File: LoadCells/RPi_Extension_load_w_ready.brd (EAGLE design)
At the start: 80 x 50 mm, 42 parts, among them U1 AD7730BRUZ, U2 AD7730BRUZ, U3 AD7730BRUZ, U4 AD7730BRUZ, U5 AD7730BRUZ, U6 AD7730BRUZ, U7 AD7730BRUZ, U8 AD7730BRUZ, U9 STM32F103RCT6, Y1 ABM3B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

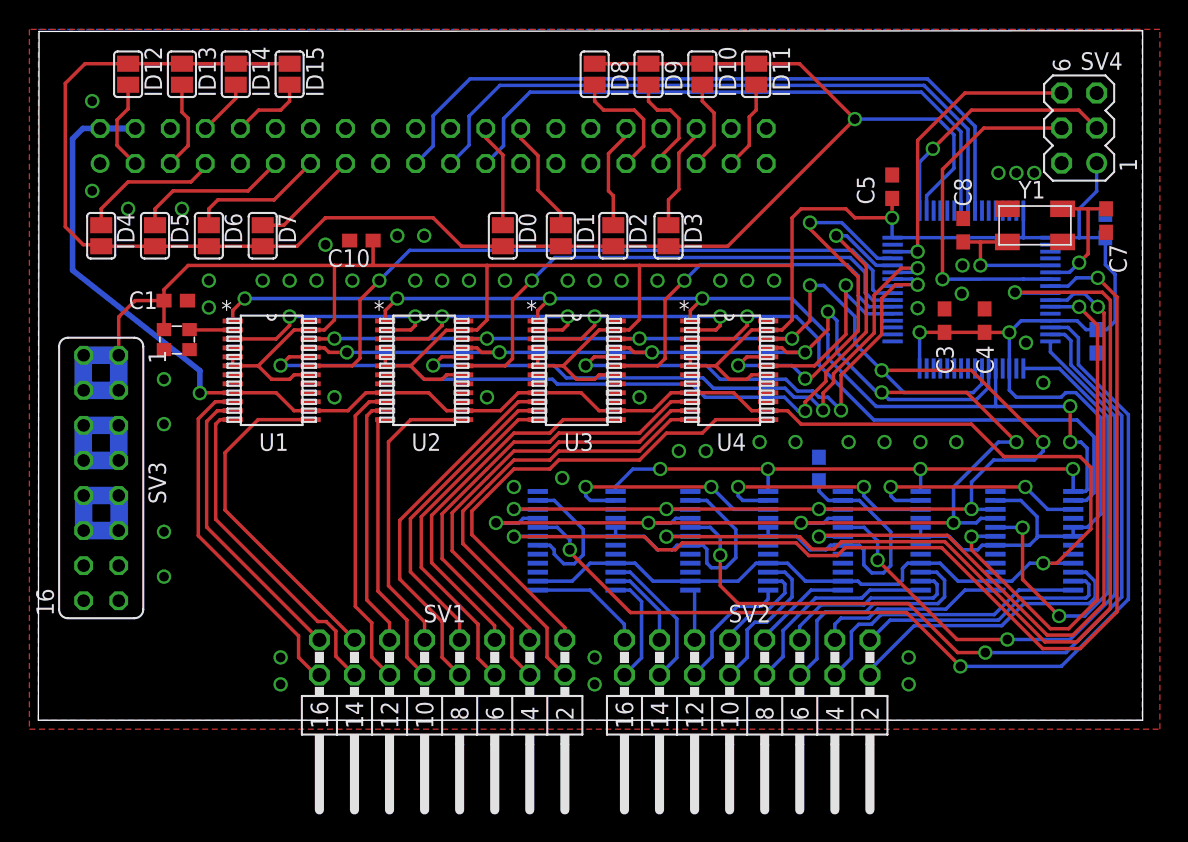
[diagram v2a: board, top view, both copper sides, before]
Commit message: added additional ground vias
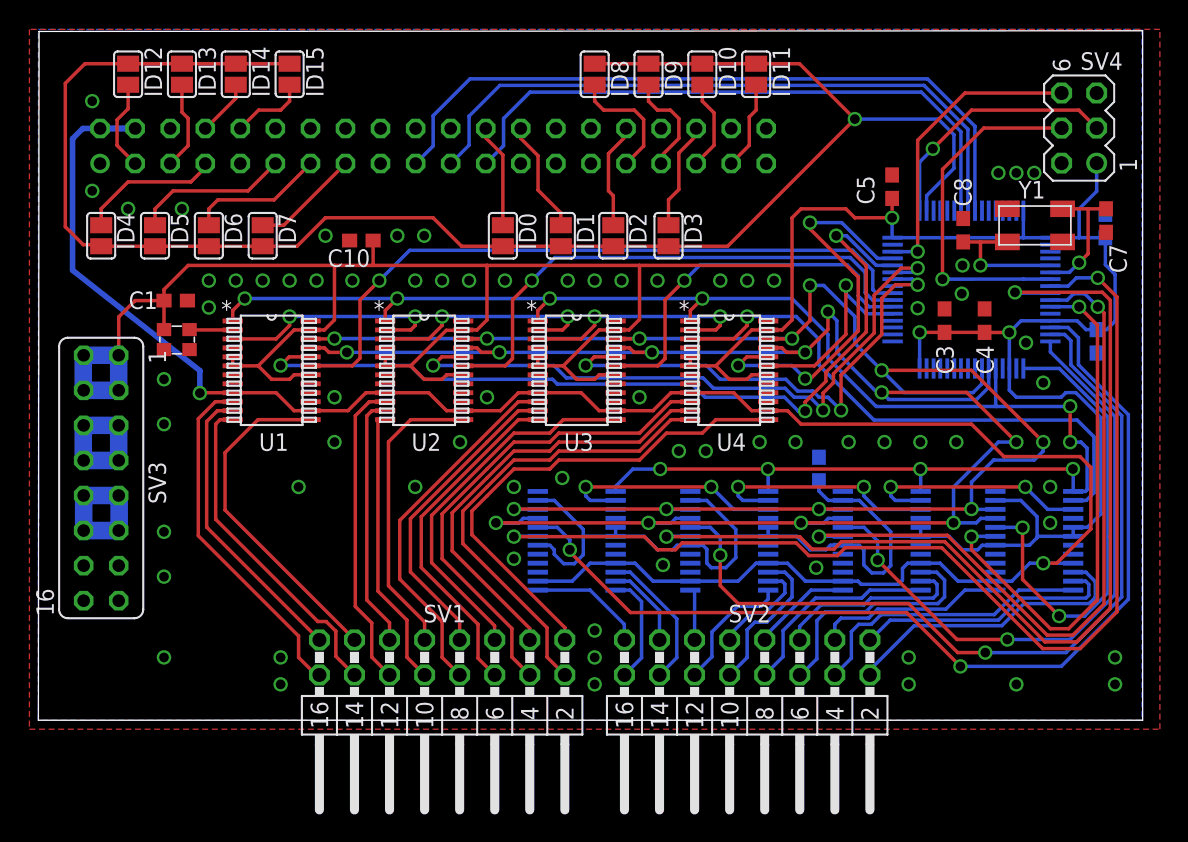
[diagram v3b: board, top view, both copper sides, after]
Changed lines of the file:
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@@
 </class>
 </classes>
-<designrules name="pban_4mil-l2">
-<description language="de">&lt;b&gt;EAGLE Design Rules&lt;/b&gt;
-&lt;p&gt;
-Die Standard-Design-Rules sind so gewählt, dass sie für
-die meisten Anwendungen passen. Sollte ihre Platine
-besondere Anforderungen haben, treffen Sie die erforderlichen
-Einstellungen hier und speichern die Design Rules unter
-einem neuen Namen ab.</description>
-<description language="en">&lt;b&gt;EAGLE Design Rules&lt;/b&gt;
-&lt;p&gt;
-The default Design Rules have been set to cover
-a wide range of applications. Your particular design
-may have different requirements, so please make the
-necessary adjustments and save your customized
-design rules under a new name.</description>
+<designrules name="dirt_cheap_dirty_boards.v1">
+<description language="en">&lt;b&gt;Dirty Cheap Dirty Board Design Rules&lt;/b&gt;
+&lt;br&gt;
+&lt;br&gt;Min width/Spacing: 5/5mil
+&lt;br&gt;Min diameter of finished hole 12mil</description>
 <param name="layerSetup" value="(1*16)"/>
-<param name="mtCopper" value="0.035mm 0.035mm 0.035mm 0.035mm 0.035mm 0.035mm 0.035mm 0.035mm 0.035mm 0.035mm 0.035mm 0.035mm 0.035mm 0.035mm 0.035mm 0.035mm"/>
-<param name="mtIsolate" value="1.53mm 1.5mm 0.2mm 0.15mm 0.2mm 0.15mm 0.2mm 0.15mm 0.2mm 0.15mm 0.2mm 0.15mm 0.2mm 0.15mm 0.2mm"/>
-<param name="mdWireWire" value="0.1mm"/>
-<param name="mdWirePad" value="0.229mm"/>
-<param name="mdWireVia" value="0.229mm"/>
-<param name="mdPadPad" value="0.1mm"/>
-<param name="mdPadVia" value="0.229mm"/>
-<param name="mdViaVia" value="0.1mm"/>
-<param name="mdSmdPad" value="0.1mm"/>
-<param name="mdSmdVia" value="0.1mm"/>
-<param name="mdSmdSmd" value="0.1mm"/>
-<param name="mdViaViaSameLayer" value="5mil"/>
+<param name="mtCopper" value="0.035mm 0.0175mm 0.035mm 0.035mm 0.035mm 0.035mm 0.035mm 0.035mm 0.035mm 0.035mm 0.035mm 0.035mm 0.035mm 0.035mm 0.0175mm 0.035mm"/>
+<param name="mtIsolate" value="1.5mm 1.1mm 0.2mm 0.15mm 0.2mm 0.15mm 0.2mm 0.15mm 0.2mm 0.15mm 0.2mm 0.15mm 0.2mm 0.15mm 0.2mm"/>
+<param name="mdWireWire" value="5mil"/>
+<param name="mdWirePad" value="5mil"/>
+<param name="mdWireVia" value="5mil"/>
+<param name="mdPadPad" value="5mil"/>
+<param name="mdPadVia" value="5mil"/>
+<param name="mdViaVia" value="5mil"/>
+<param name="mdSmdPad" value="0mil"/>
+<param name="mdSmdVia" value="0mil"/>
+<param name="mdSmdSmd" value="0mil"/>
+<param name="mdViaViaSameLayer" value="8mil"/>
 <param name="mnLayersViaInSmd" value="2"/>
-<param name="mdCopperDimension" value="0.5mm"/>
-<param name="mdDrill" value="0.5mm"/>
+<param name="mdCopperDimension" value="10mil"/>
+<param name="mdDrill" value="10mil"/>
 <param name="mdSmdStop" value="0mil"/>
-<param name="msWidth" value="0.1mm"/>
-<param name="msDrill" value="0.3mm"/>
-<param name="msMicroVia" value="0.1mm"/>
-<param name="msBlindViaRatio" value="0.76"/>
+<param name="msWidth" value="5mil"/>
+<param name="msDrill" value="12mil"/>
+<param name="msMicroVia" value="12mil"/>
+<param name="msBlindViaRatio" value="0.5"/>
 <param name="rvPadTop" value="0.25"/>
 <param name="rvPadInner" value="0.25"/>
@@
 <param name="rvMicroViaOuter" value="0.25"/>
 <param name="rvMicroViaInner" value="0.25"/>
-<param name="rlMinPadTop" value="0.15mm"/>
-<param name="rlMaxPadTop" value="0.5mm"/>
-<param name="rlMinPadInner" value="0.2mm"/>
-<param name="rlMaxPadInner" value="0.5mm"/>
-<param name="rlMinPadBottom" value="0.15mm"/>
-<param name="rlMaxPadBottom" value="0.5mm"/>
-<param name="rlMinViaOuter" value="0.15mm"/>
-<param name="rlMaxViaOuter" value="0.5mm"/>
-<param name="rlMinViaInner" value="0.2mm"/>
-<param name="rlMaxViaInner" value="0.5mm"/>
-<param name="rlMinMicroViaOuter" value="0.1mm"/>
-<param name="rlMaxMicroViaOuter" value="0.5mm"/>
-<param name="rlMinMicroViaInner" value="0.1mm"/>
-<param name="rlMaxMicroViaInner" value="0.5mm"/>
+<param name="rlMinPadTop" value="10mil"/>
+<param name="rlMaxPadTop" value="20mil"/>
+<param name="rlMinPadInner" value="10mil"/>
+<param name="rlMaxPadInner" value="20mil"/>
+<param name="rlMinPadBottom" value="10mil"/>
+<param name="rlMaxPadBottom" value="20mil"/>
+<param name="rlMinViaOuter" value="6mil"/>
+<param name="rlMaxViaOuter" value="20mil"/>
+<param name="rlMinViaInner" value="6mil"/>
+<param name="rlMaxViaInner" value="20mil"/>
+<param name="rlMinMicroViaOuter" value="4mil"/>
+<param name="rlMaxMicroViaOuter" value="20mil"/>
+<param name="rlMinMicroViaInner" value="4mil"/>
+<param name="rlMaxMicroViaInner" value="20mil"/>
 <param name="psTop" value="-1"/>
 <param name="psBottom" value="-1"/>
-<param name="psFirst" value="-1"/>
+<param name="psFirst" value="0"/>
 <param name="psElongationLong" value="100"/>
 <param name="psElongationOffset" value="100"/>
 <param name="mvStopFrame" value="1"/>
 <param name="mvCreamFrame" value="0"/>
-<param name="mlMinStopFrame" value="4mil"/>
-<param name="mlMaxStopFrame" value="4mil"/>
+<param name="mlMinStopFrame" value="2mil"/>
+<param name="mlMaxStopFrame" value="2mil"/>
 <param name="mlMinCreamFrame" value="0mil"/>
 <param name="mlMaxCreamFrame" value="0mil"/>
-<param name="mlViaStopLimit" value="0.35mm"/>
+<param name="mlViaStopLimit" value="25mil"/>
 <param name="srRoundness" value="0"/>
 <param name="srMinRoundness" value="0mil"/>
@@
 <param name="checkAngle" value="0"/>
 <param name="checkFont" value="1"/>
-<param name="checkRestrict" value="1"/>
+<param name="checkRestrict" value="0"/>
 <param name="useDiameter" value="13"/>
 <param name="maxErrors" value="50"/>
@@
 <via x="51.35" y="31.85" extent="1-16" drill="0.7"/>
 <via x="49.4" y="31.85" extent="1-16" drill="0.7"/>
-<via x="20.8" y="34.45" extent="1-16" drill="0.7"/>
+<via x="20.8" y="35.1" extent="1-16" drill="0.7"/>
 <via x="26" y="35.1" extent="1-16" drill="0.7"/>
 <via x="27.95" y="35.1" extent="1-16" drill="0.7"/>
@@
 <via x="9.1" y="13.65" extent="1-16" drill="0.7"/>
 <via x="9.1" y="10.4" extent="1-16" drill="0.7"/>
-<wire x1="74.9694" y1="14.625" x2="74.9694" y2="12.025" width="0" layer="19" extent="16-16"/>
+<via x="70.85" y="2.6" extent="1-16" drill="0.7"/>
+<via x="78" y="2.6" extent="1-16" drill="0.7"/>
+<via x="78" y="4.55" extent="1-16" drill="0.7"/>
+<via x="9.1" y="4.55" extent="1-16" drill="0.7"/>
+<via x="34.45" y="11.7" extent="1-16" drill="0.7"/>
+<via x="40.3" y="6.5" extent="1-16" drill="0.7"/>
+<via x="73.3" y="14.3" extent="1-16" drill="0.7"/>
+<via x="73.3" y="16.9" extent="1-16" drill="0.7"/>
+<via x="45.25" y="11.25" extent="1-16" drill="0.7"/>
+<via x="56.35" y="11.05" extent="1-16" drill="0.7"/>
+<via x="14.3" y="31.85" extent="1-16" drill="0.7"/>
+<via x="21.45" y="20.15" extent="1-16" drill="0.7"/>
+<via x="30.55" y="20.15" extent="1-16" drill="0.7"/>
+<via x="18.85" y="16.9" extent="1-16" drill="0.7"/>
+<via x="27.3" y="16.9" extent="1-16" drill="0.7"/>
 </signal>
 <signal name="DVCC">

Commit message: disconnected shorting ground connection on connector board
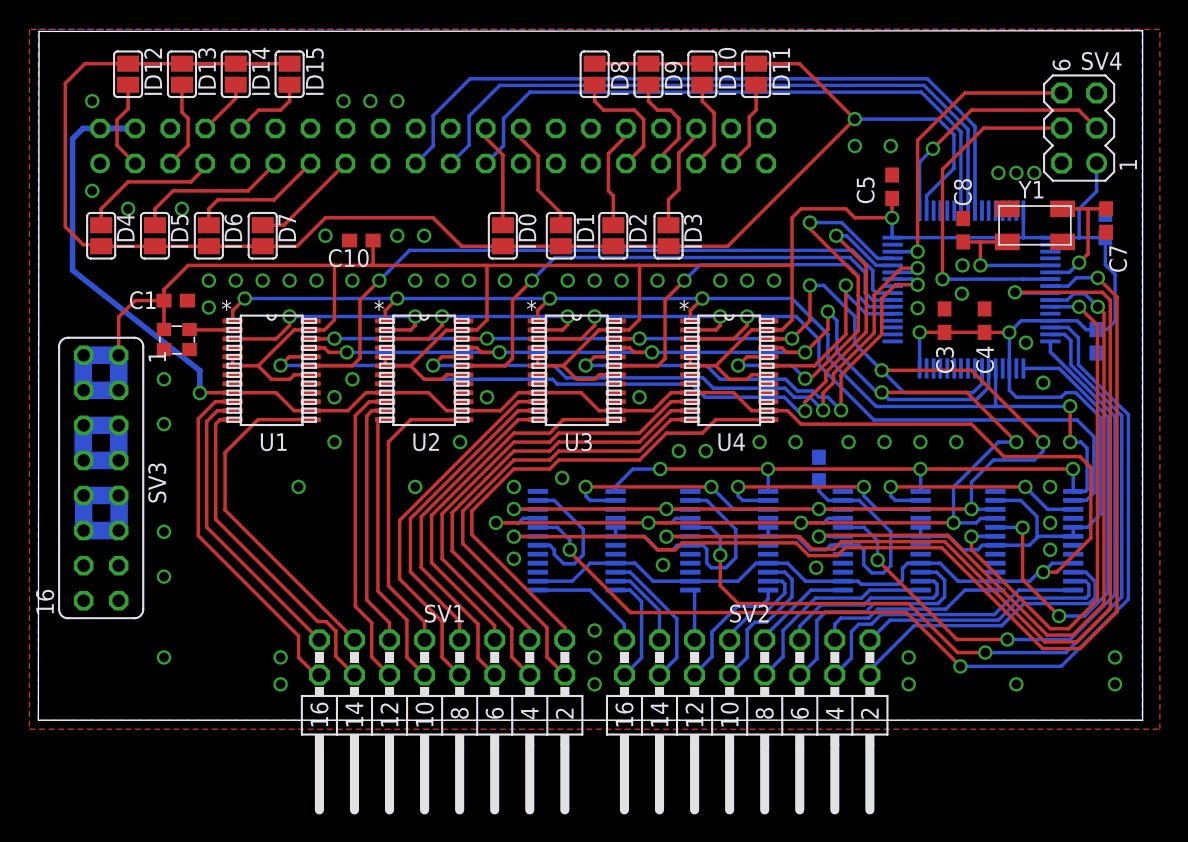
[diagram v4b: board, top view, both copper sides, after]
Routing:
- net +5V: track 152.5 -> 153.1 mm
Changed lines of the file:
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@@
 <via x="18.85" y="16.9" extent="1-16" drill="0.7"/>
 <via x="27.3" y="16.9" extent="1-16" drill="0.7"/>
+<via x="59.15" y="41.6" extent="1-16" drill="0.7"/>
+<via x="61.75" y="41.6" extent="1-16" drill="0.7"/>
+<via x="22.1" y="44.85" extent="1-16" drill="0.7"/>
+<via x="24.05" y="44.85" extent="1-16" drill="0.7"/>
+<via x="26" y="44.85" extent="1-16" drill="0.7"/>
+<via x="22.75" y="24.7" extent="1-16" drill="0.7"/>
+<via x="73.3" y="12.35" extent="1-16" drill="0.7"/>
 </signal>
 <signal name="DVCC">
@@
 <contactref element="U5" pad="9"/>
 <contactref element="U5" pad="14"/>
-<wire x1="72.8" y1="11.375003125" x2="71.825003125" y2="11.375003125" width="0.254" layer="16"/>
-<wire x1="71.825003125" y1="11.375003125" x2="70.525" y2="10.075" width="0.254" layer="16"/>
-<wire x1="69.3306" y1="10.075" x2="70.525" y2="10.075" width="0.254" layer="16"/>
+<wire x1="72.8" y1="10.725003125" x2="72.475003125" y2="10.725003125" width="0.254" layer="16"/>
+<wire x1="72.475003125" y1="10.725003125" x2="71.825" y2="10.075" width="0.254" layer="16"/>
+<wire x1="69.3306" y1="10.075" x2="71.825" y2="10.075" width="0.254" layer="16"/>
 <contactref element="U6" pad="9"/>
 <contactref element="U6" pad="14"/>
@@
 <wire x1="69.95" y1="19.1" x2="75.465115625" y2="19.1" width="0.254" layer="1"/>
 <wire x1="75.465115625" y1="19.1" x2="76.2464875" y2="18.318628125" width="0.254" layer="1"/>
-<wire x1="76.2464875" y1="18.318628125" x2="76.2464875" y2="13.846484375" width="0.254" layer="1"/>
-<wire x1="76.2464875" y1="13.846484375" x2="73.775003125" y2="11.375003125" width="0.254" layer="1"/>
+<wire x1="76.2464875" y1="18.318628125" x2="76.2464875" y2="13.196484375" width="0.254" layer="1"/>
+<wire x1="76.2464875" y1="13.196484375" x2="73.775003125" y2="10.725003125" width="0.254" layer="1"/>
 <contactref element="U7" pad="9"/>
 <contactref element="U7" pad="14"/>
@@
 <wire x1="36.1806" y1="10.075" x2="38.675" y2="10.075" width="0.254" layer="16"/>
 <wire x1="38.675" y1="10.075" x2="39.975003125" y2="11.375003125" width="0.254" layer="16"/>
-<via x="72.8" y="11.375003125" extent="1-16" drill="0.7"/>
-<wire x1="72.8" y1="11.375003125" x2="74.9694" y2="11.375003125" width="0.254" layer="16"/>
-<wire x1="72.8" y1="11.375003125" x2="73.775003125" y2="11.375003125" width="0.254" layer="1"/>
+<via x="72.8" y="10.725003125" extent="1-16" drill="0.7"/>
+<wire x1="72.8" y1="10.725003125" x2="73.775003125" y2="10.725003125" width="0.254" layer="1"/>
 <wire x1="52.8694" y1="22.425" x2="54.275" y2="22.425" width="0.254" layer="1"/>
 <wire x1="54.275" y1="22.425" x2="55.25" y2="21.45" width="0.254" layer="1"/>
@@
 <wire x1="62.6" y1="11" x2="62.975003125" y2="11.375003125" width="0.254" layer="16"/>
 <wire x1="59.6" y1="9.85" x2="59.375" y2="10.075" width="0.254" layer="16"/>
+<wire x1="74.9694" y1="11.375003125" x2="73.45" y2="11.375003125" width="0.254" layer="16"/>
+<wire x1="73.45" y1="11.375003125" x2="72.8" y2="10.725003125" width="0.254" layer="16"/>
 </signal>
 <signal name="SWDIO">
